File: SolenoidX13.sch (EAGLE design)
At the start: 26 parts, among them J1 SAMTEC-CLT-111-01-X-DJ, U1 ULN2003V12

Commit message: Pretty much ready for production (owo)
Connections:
- net +3V3: now also J1.4; no longer J1.6
- net GND: now also J1.6; no longer J1.4
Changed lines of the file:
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@@
-</segment>
-<segment>
-<wire x1="215.9" y1="104.14" x2="226.06" y2="104.14" width="0.1524" layer="91"/>
-<label x="220.98" y="104.14" size="1.778" layer="95"/>
-<pinref part="J1" gate="A" pin="4"/>
 </segment>
 <segment>
@@
 <label x="220.98" y="93.98" size="1.778" layer="95"/>
 <pinref part="J1" gate="A" pin="12"/>
+</segment>
+<segment>
+<wire x1="215.9" y1="101.6" x2="226.06" y2="101.6" width="0.1524" layer="91"/>
+<label x="220.98" y="101.6" size="1.778" layer="95"/>
+<pinref part="J1" gate="A" pin="6"/>
 </segment>
 </net>
@@
 </segment>
 <segment>
-<wire x1="215.9" y1="101.6" x2="226.06" y2="101.6" width="0.1524" layer="91"/>
-<label x="220.98" y="101.6" size="1.778" layer="95"/>
-<pinref part="J1" gate="A" pin="6"/>
+<wire x1="215.9" y1="104.14" x2="226.06" y2="104.14" width="0.1524" layer="91"/>
+<label x="220.98" y="104.14" size="1.778" layer="95"/>
+<pinref part="J1" gate="A" pin="4"/>
 </segment>
 </net>

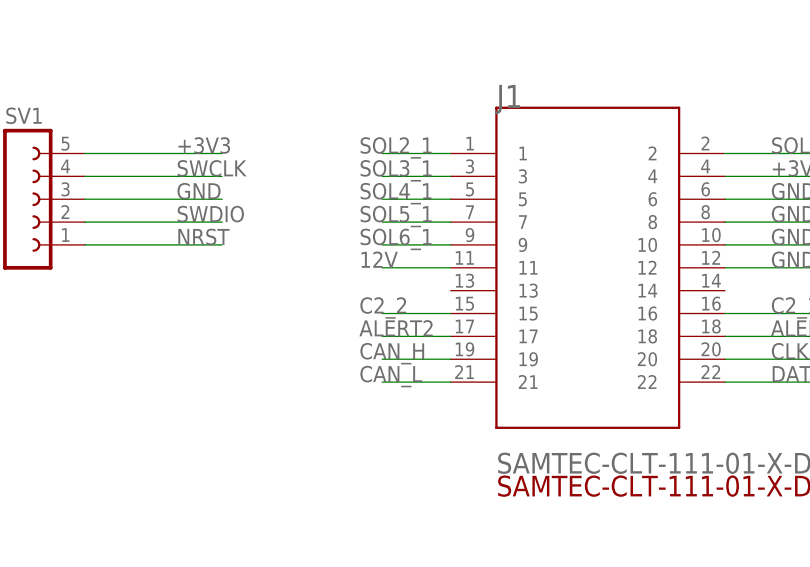
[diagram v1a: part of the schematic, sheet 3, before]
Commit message: Added nrst pin to connector and routed
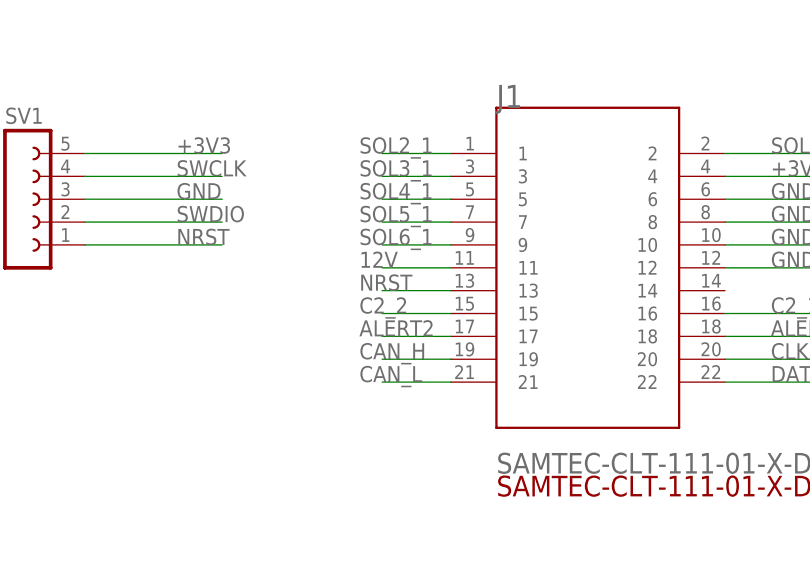
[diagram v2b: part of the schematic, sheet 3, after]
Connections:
- net NRST: now also J1.13
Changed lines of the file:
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@@
 <label x="154.94" y="96.52" size="1.778" layer="95"/>
+</segment>
+<segment>
+<wire x1="185.42" y1="91.44" x2="177.8" y2="91.44" width="0.1524" layer="91"/>
+<label x="175.26" y="91.44" size="1.778" layer="95"/>
+<pinref part="J1" gate="A" pin="13"/>
 </segment>
 </net>

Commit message: added an OWO
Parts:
- renumbered U$1 to RESET, U$3 to STM
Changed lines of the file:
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@@
 <part name="GND" library="supply2" library_urn="urn:adsk.eagle:library:372" deviceset="GND" device=""/>
 <part name="+3V1" library="supply1" library_urn="urn:adsk.eagle:library:371" deviceset="+3V3" device=""/>
-<part name="U$3" library="PI_Shield_Library" deviceset="STM32F042K6T6" device=""/>
+<part name="STM" library="PI_Shield_Library" deviceset="STM32F042K6T6" device=""/>
 <part name="GND1" library="supply2" library_urn="urn:adsk.eagle:library:372" deviceset="GND" device=""/>
 <part name="GND2" library="supply2" library_urn="urn:adsk.eagle:library:372" deviceset="GND" device=""/>
@@
 <part name="J1" library="SAMTEC-CLT-111-01-X-D" deviceset="SAMTEC-CLT-111-01-X-D" device="J"/>
 <part name="SV1" library="con-lsta" library_urn="urn:adsk.eagle:library:161" deviceset="FE05-1" device="" package3d_urn="urn:adsk.eagle:package:8190/1"/>
-<part name="U$1" library="Push button - FSM2JMTR" deviceset="DISCRETECOMPONENTS_SWITCH" device="" package3d_urn="urn:adsk.eagle:package:24384574/2"/>
+<part name="RESET" library="Push button - FSM2JMTR" deviceset="DISCRETECOMPONENTS_SWITCH" device="" package3d_urn="urn:adsk.eagle:package:24384574/2"/>
 <part name="R4" library="SparkFun-Resistors" library_urn="urn:adsk.eagle:library:532" deviceset="4.7KOHM" device="-0603-1/10W-1%" package3d_urn="urn:adsk.eagle:package:39650/1" value="4.7k"/>
 <part name="R5" library="SparkFun-Resistors" library_urn="urn:adsk.eagle:library:532" deviceset="4.7KOHM" device="-0603-1/10W-1%" package3d_urn="urn:adsk.eagle:package:39650/1" value="4.7k"/>
@@
 <attribute name="VALUE" x="147.32" y="111.76" size="1.778" layer="96" rot="R90"/>
 </instance>
-<instance part="U$3" gate="G$1" x="93.98" y="93.98" smashed="yes">
+<instance part="STM" gate="G$1" x="93.98" y="93.98" smashed="yes">
 <attribute name="NAME" x="76.2" y="121.92" size="2.54" layer="94"/>
 </instance>
@@
 <attribute name="VALUE" x="53.34" y="104.14" size="1.778" layer="96" rot="R90"/>
 </instance>
-<instance part="U$1" gate="G$1" x="30.48" y="88.9" smashed="yes" rot="R90"/>
+<instance part="RESET" gate="G$1" x="30.48" y="88.9" smashed="yes" rot="R90"/>
 <instance part="R4" gate="G$1" x="111.76" y="55.88" smashed="yes">
 <attribute name="NAME" x="111.76" y="57.404" size="1.778" layer="95" font="vector" align="bottom-center"/>
@@
 </segment>
 <segment>
-<pinref part="U$3" gate="G$1" pin="VSS1"/>
+<pinref part="STM" gate="G$1" pin="VSS1"/>
 <wire x1="83.82" y1="116.84" x2="83.82" y2="121.92" width="0.1524" layer="91"/>
 <pinref part="GND1" gate="GND" pin="GND"/>
 <wire x1="83.82" y1="121.92" x2="71.12" y2="121.92" width="0.1524" layer="91"/>
 <wire x1="71.12" y1="121.92" x2="71.12" y2="119.38" width="0.1524" layer="91"/>
-<pinref part="U$3" gate="G$1" pin="PB8-BOOT0"/>
+<pinref part="STM" gate="G$1" pin="PB8-BOOT0"/>
 <wire x1="86.36" y1="116.84" x2="86.36" y2="121.92" width="0.1524" layer="91"/>
 <wire x1="86.36" y1="121.92" x2="83.82" y2="121.92" width="0.1524" layer="91"/>
@@
 </segment>
 <segment>
-<pinref part="U$3" gate="G$1" pin="VSS"/>
+<pinref part="STM" gate="G$1" pin="VSS"/>
 <pinref part="GND2" gate="GND" pin="GND"/>
 <wire x1="104.14" y1="71.12" x2="104.14" y2="66.04" width="0.1524" layer="91"/>
@@
 <wire x1="30.48" y1="81.28" x2="17.78" y2="81.28" width="0.1524" layer="91"/>
 <junction x="17.78" y="81.28"/>
-<pinref part="U$1" gate="G$1" pin="P$1"/>
+<pinref part="RESET" gate="G$1" pin="P$1"/>
 </segment>
 <segment>
@@
 </segment>
 <segment>
-<pinref part="U$3" gate="G$1" pin="VDDIO2"/>
+<pinref part="STM" gate="G$1" pin="VDDIO2"/>
 <wire x1="116.84" y1="83.82" x2="134.62" y2="83.82" width="0.1524" layer="91"/>
 <label x="129.54" y="83.82" size="1.778" layer="95"/>
 </segment>
 <segment>
-<pinref part="U$3" gate="G$1" pin="VDDA"/>
+<pinref part="STM" gate="G$1" pin="VDDA"/>
 <wire x1="71.12" y1="91.44" x2="55.88" y2="91.44" width="0.1524" layer="91"/>
 <label x="55.88" y="91.44" size="1.778" layer="95"/>
 </segment>
 <segment>
-<pinref part="U$3" gate="G$1" pin="VDD"/>
+<pinref part="STM" gate="G$1" pin="VDD"/>
 <wire x1="71.12" y1="104.14" x2="55.88" y2="104.14" width="0.1524" layer="91"/>
 <pinref part="+3V4" gate="G$1" pin="+3V3"/>
@@
 <net name="CAN_TX" class="0">
 <segment>
-<pinref part="U$3" gate="G$1" pin="PA12"/>
+<pinref part="STM" gate="G$1" pin="PA12"/>
 <wire x1="116.84" y1="99.06" x2="132.08" y2="99.06" width="0.1524" layer="91"/>
 <label x="127" y="99.06" size="1.778" layer="95"/>
@@
 <net name="CAN_RX" class="0">
 <segment>
-<pinref part="U$3" gate="G$1" pin="PA11"/>
+<pinref part="STM" gate="G$1" pin="PA11"/>
 <wire x1="116.84" y1="96.52" x2="132.08" y2="96.52" width="0.1524" layer="91"/>
 <label x="127" y="96.52" size="1.778" layer="95"/>
@@
 <wire x1="17.78" y1="96.52" x2="17.78" y2="91.44" width="0.1524" layer="91"/>
 <junction x="17.78" y="96.52"/>
-<pinref part="U$3" gate="G$1" pin="NRST"/>
+<pinref part="STM" gate="G$1" pin="NRST"/>
 <wire x1="17.78" y1="96.52" x2="30.48" y2="96.52" width="0.1524" layer="91"/>
 <wire x1="30.48" y1="96.52" x2="71.12" y2="96.52" width="0.1524" layer="91"/>
 <wire x1="17.78" y1="101.6" x2="17.78" y2="96.52" width="0.1524" layer="91"/>
-<pinref part="U$1" gate="G$1" pin="P$2"/>
+<pinref part="RESET" gate="G$1" pin="P$2"/>
 <junction x="30.48" y="96.52"/>
 <label x="58.42" y="96.52" size="1.778" layer="95"/>
@@
 <net name="LED" class="0">
 <segment>
-<pinref part="U$3" gate="G$1" pin="PA15"/>
+<pinref part="STM" gate="G$1" pin="PA15"/>
 <wire x1="104.14" y1="116.84" x2="104.14" y2="129.54" width="0.1524" layer="91"/>
 <label x="104.14" y="121.92" size="1.778" layer="95" rot="R90"/>
@@
 <wire x1="71.12" y1="86.36" x2="66.04" y2="86.36" width="0.1524" layer="91"/>
 <label x="68.58" y="86.36" size="1.778" layer="95" rot="R180"/>
-<pinref part="U$3" gate="G$1" pin="PA1"/>
+<pinref part="STM" gate="G$1" pin="PA1"/>
 </segment>
 </net>
@@
 <wire x1="91.44" y1="60.96" x2="91.44" y2="71.12" width="0.1524" layer="91"/>
 <label x="91.44" y="60.96" size="1.778" layer="95" rot="R90"/>
-<pinref part="U$3" gate="G$1" pin="PA6"/>
+<pinref part="STM" gate="G$1" pin="PA6"/>
 </segment>
 </net>
@@
 <wire x1="71.12" y1="83.82" x2="66.04" y2="83.82" width="0.1524" layer="91"/>
 <label x="68.58" y="83.82" size="1.778" layer="95" rot="R180"/>
-<pinref part="U$3" gate="G$1" pin="PA2"/>
+<pinref part="STM" gate="G$1" pin="PA2"/>
 </segment>
 </net>
@@
 <wire x1="83.82" y1="60.96" x2="83.82" y2="71.12" width="0.1524" layer="91"/>
 <label x="83.82" y="60.96" size="1.778" layer="95" rot="R90"/>
-<pinref part="U$3" gate="G$1" pin="PA3"/>
+<pinref part="STM" gate="G$1" pin="PA3"/>
 </segment>
 </net>
@@
 <wire x1="86.36" y1="60.96" x2="86.36" y2="71.12" width="0.1524" layer="91"/>
 <label x="86.36" y="60.96" size="1.778" layer="95" rot="R90"/>
-<pinref part="U$3" gate="G$1" pin="PA4"/>
+<pinref part="STM" gate="G$1" pin="PA4"/>
 </segment>
 </net>
@@
 <wire x1="88.9" y1="60.96" x2="88.9" y2="71.12" width="0.1524" layer="91"/>
 <label x="88.9" y="60.96" size="1.778" layer="95" rot="R90"/>
-<pinref part="U$3" gate="G$1" pin="PA5"/>
+<pinref part="STM" gate="G$1" pin="PA5"/>
 </segment>
 </net>
@@
 <wire x1="71.12" y1="88.9" x2="66.04" y2="88.9" width="0.1524" layer="91"/>
 <label x="68.58" y="88.9" size="1.778" layer="95" rot="R180"/>
-<pinref part="U$3" gate="G$1" pin="PA0"/>
+<pinref part="STM" gate="G$1" pin="PA0"/>
 </segment>
 </net>
@@
 <wire x1="116.84" y1="91.44" x2="132.08" y2="91.44" width="0.1524" layer="91"/>
 <label x="127" y="91.44" size="1.778" layer="95"/>
-<pinref part="U$3" gate="G$1" pin="PA10"/>
+<pinref part="STM" gate="G$1" pin="PA10"/>
 </segment>
 </net>
@@
 <wire x1="116.84" y1="88.9" x2="132.08" y2="88.9" width="0.1524" layer="91"/>
 <label x="127" y="88.9" size="1.778" layer="95"/>
-<pinref part="U$3" gate="G$1" pin="PA9"/>
+<pinref part="STM" gate="G$1" pin="PA9"/>
 </segment>
 </net>
@@
 <wire x1="96.52" y1="60.96" x2="96.52" y2="71.12" width="0.1524" layer="91"/>
 <label x="96.52" y="60.96" size="1.778" layer="95" rot="R90"/>
-<pinref part="U$3" gate="G$1" pin="PA7"/>
+<pinref part="STM" gate="G$1" pin="PA7"/>
 </segment>
 </net>
@@
 <wire x1="99.06" y1="121.92" x2="99.06" y2="116.84" width="0.1524" layer="91"/>
 <label x="99.06" y="119.38" size="1.778" layer="95" rot="R90"/>
-<pinref part="U$3" gate="G$1" pin="PB4"/>
+<pinref part="STM" gate="G$1" pin="PB4"/>
 </segment>
 </net>
@@
 <wire x1="101.6" y1="121.92" x2="101.6" y2="116.84" width="0.1524" layer="91"/>
 <label x="101.6" y="119.38" size="1.778" layer="95" rot="R90"/>
-<pinref part="U$3" gate="G$1" pin="PB3"/>
+<pinref part="STM" gate="G$1" pin="PB3"/>
 </segment>
 </net>
@@
 <wire x1="116.84" y1="104.14" x2="132.08" y2="104.14" width="0.1524" layer="91"/>
 <label x="127" y="104.14" size="1.778" layer="95"/>
-<pinref part="U$3" gate="G$1" pin="PA14"/>
+<pinref part="STM" gate="G$1" pin="PA14"/>
 </segment>
 </net>
@@
 <wire x1="116.84" y1="101.6" x2="132.08" y2="101.6" width="0.1524" layer="91"/>
 <label x="127" y="101.6" size="1.778" layer="95"/>
-<pinref part="U$3" gate="G$1" pin="PA13"/>
+<pinref part="STM" gate="G$1" pin="PA13"/>
 </segment>
 </net>
@@
 <net name="N$1" class="0">
 <segment>
-<pinref part="U$3" gate="G$1" pin="PB1"/>
+<pinref part="STM" gate="G$1" pin="PB1"/>
 <wire x1="101.6" y1="71.12" x2="101.6" y2="55.88" width="0.1524" layer="91"/>
 <pinref part="R4" gate="G$1" pin="1"/>
@@
 <net name="N$2" class="0">
 <segment>
-<pinref part="U$3" gate="G$1" pin="PB0"/>
+<pinref part="STM" gate="G$1" pin="PB0"/>
 <wire x1="99.06" y1="71.12" x2="99.06" y2="48.26" width="0.1524" layer="91"/>
 <pinref part="R5" gate="G$1" pin="1"/>

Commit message: ground plane? more like ground pain
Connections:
- net GND: no longer J1.12
- net SWCLK: now also J1.12
- net SWDIO: now also J1.14
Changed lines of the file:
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@@
-</segment>
-<segment>
-<wire x1="215.9" y1="93.98" x2="226.06" y2="93.98" width="0.1524" layer="91"/>
-<label x="220.98" y="93.98" size="1.778" layer="95"/>
-<pinref part="J1" gate="A" pin="12"/>
 </segment>
 <segment>
@@
 <label x="154.94" y="99.06" size="1.778" layer="95"/>
 </segment>
+<segment>
+<wire x1="215.9" y1="91.44" x2="231.14" y2="91.44" width="0.1524" layer="91"/>
+<label x="226.06" y="91.44" size="1.778" layer="95"/>
+<pinref part="J1" gate="A" pin="14"/>
+</segment>
 </net>
 <net name="SWCLK" class="0">
@@
 <label x="154.94" y="104.14" size="1.778" layer="95"/>
 </segment>
+<segment>
+<wire x1="215.9" y1="93.98" x2="231.14" y2="93.98" width="0.1524" layer="91"/>
+<label x="226.06" y="93.98" size="1.778" layer="95"/>
+<pinref part="J1" gate="A" pin="12"/>
+</segment>
 </net>

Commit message: grant stuff owo
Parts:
- removed C11: 0.1uF, SparkFun-Capacitors:0.1UF-0603-25V-(+80/-20%)
- removed J1: SAMTEC-CLT-111-01-X-DJ, SAMTEC-CLT-111-01-X-D:SAMTEC-CLT-111-01-X-DJ
- removed R10, R11: 1k, SparkFun-Resistors:1KOHM-0603-1/10W-1%
- added U$1: SOL-TO-BKP, Solenoid-Backplane Connector:SOL-TO-BKP
- C3, C4: value 100nF -> 4.7uF
- C5: value 0.01uF -> 4.7uF
- C6: value 1uF -> 4.7uF
- D1: value (none) -> Green
- D2: value (none) -> Orange
- D4: value (none) -> Red
- R7: value (none) -> 470
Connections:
- removed net GPIO0: STM.PA0
- removed net GPIO7: STM.PA7
- removed net N$5: C11.2, R10.1, R11.2
- net +3V3: now also U$1.3; no longer J1.4
- net 12V: now also U$1.12; no longer J1.11
- net ALERT1: now also U$1.17; no longer J1.18
- net ALERT2: now also U$1.18; no longer J1.17
- net C2_1: now also U$1.15; no longer J1.16
- net C2_2: now also U$1.16; no longer J1.15
- net CAN_H: now also U$1.20; no longer J1.19, R10.2
- net CAN_L: now also U$1.22; no longer J1.21, R11.1
- net CLK: now also U$1.19; no longer J1.20
- net DATA: now also U$1.21; no longer J1.22
- net GND: now also U$1.5, U$1.7, U$1.9; no longer C11.1, J1.10, J1.6, J1.8
- net NRST: now also U$1.14; no longer J1.13
- net SOL1_1: now also U$1.1; no longer J1.2
- net SOL2_1: now also U$1.2; no longer J1.1
- net SOL3_1: now also U$1.4; no longer J1.3
- net SOL4_1: now also U$1.6; no longer J1.5
- net SOL5_1: now also U$1.8; no longer J1.7
- net SOL6_1: now also U$1.10; no longer J1.9
- net SWCLK: now also U$1.11; no longer J1.12
- net SWDIO: now also U$1.13; no longer J1.14
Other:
- note removed: "CAN TERMINATION"
- moved on the sheet: C10, U$8
